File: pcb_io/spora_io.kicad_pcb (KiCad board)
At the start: 2 copper layers, 16.8 x 18.4 mm, 32 parts, among them CON2 VBA_IN, J1 DF12B 3.0 10DS 0.5V 81, J2 ER-OLED0.49-1Series, Q1 FDN335N_NMOS, Q2 FDN338P_PMOS, SW1 SW_PUSH, SW2 SW_PUSH, U1 MCP1252-ADJ

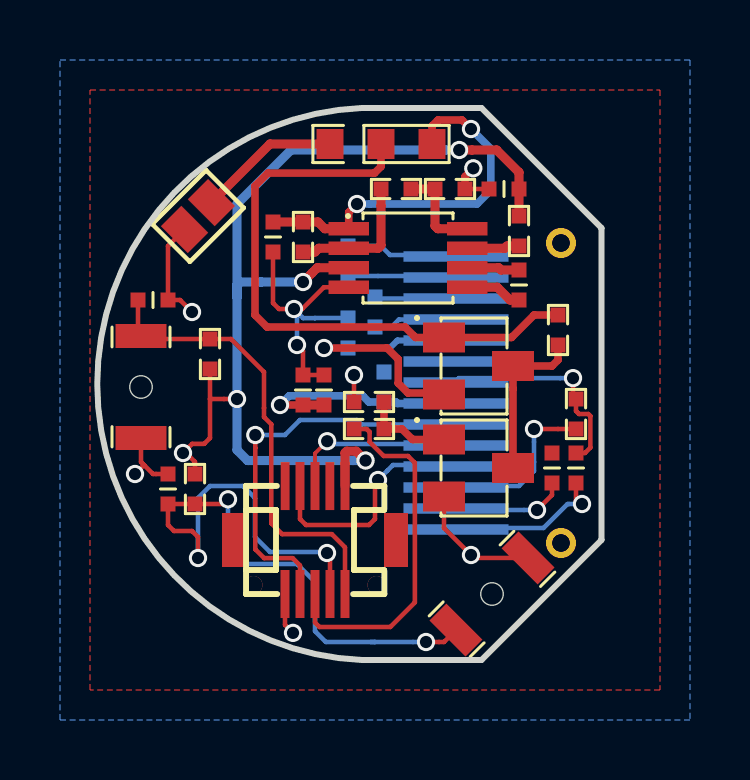
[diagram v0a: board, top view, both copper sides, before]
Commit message: Change Board color
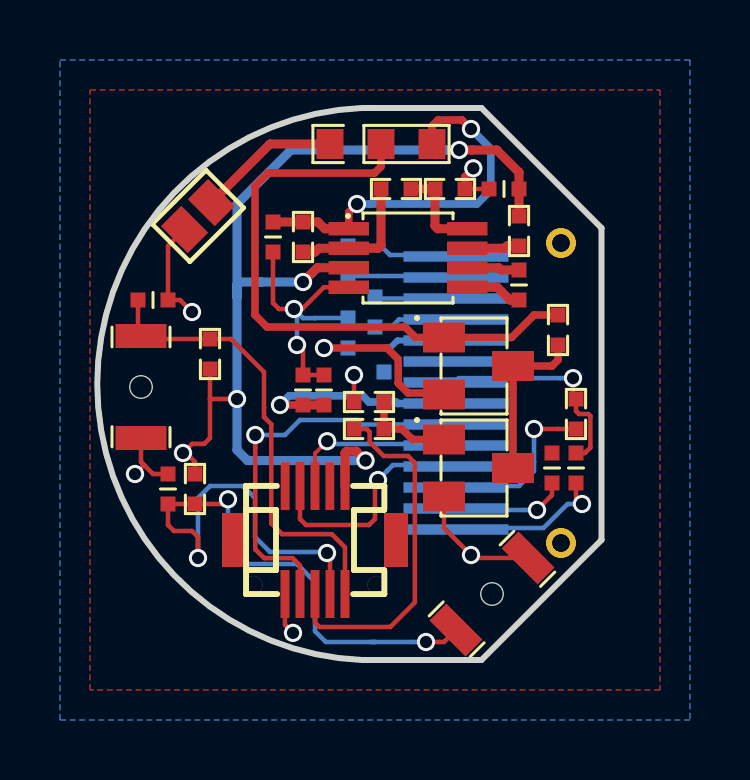
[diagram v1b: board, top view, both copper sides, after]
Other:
- net class Default removed
